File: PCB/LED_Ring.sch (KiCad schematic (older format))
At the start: 60 parts

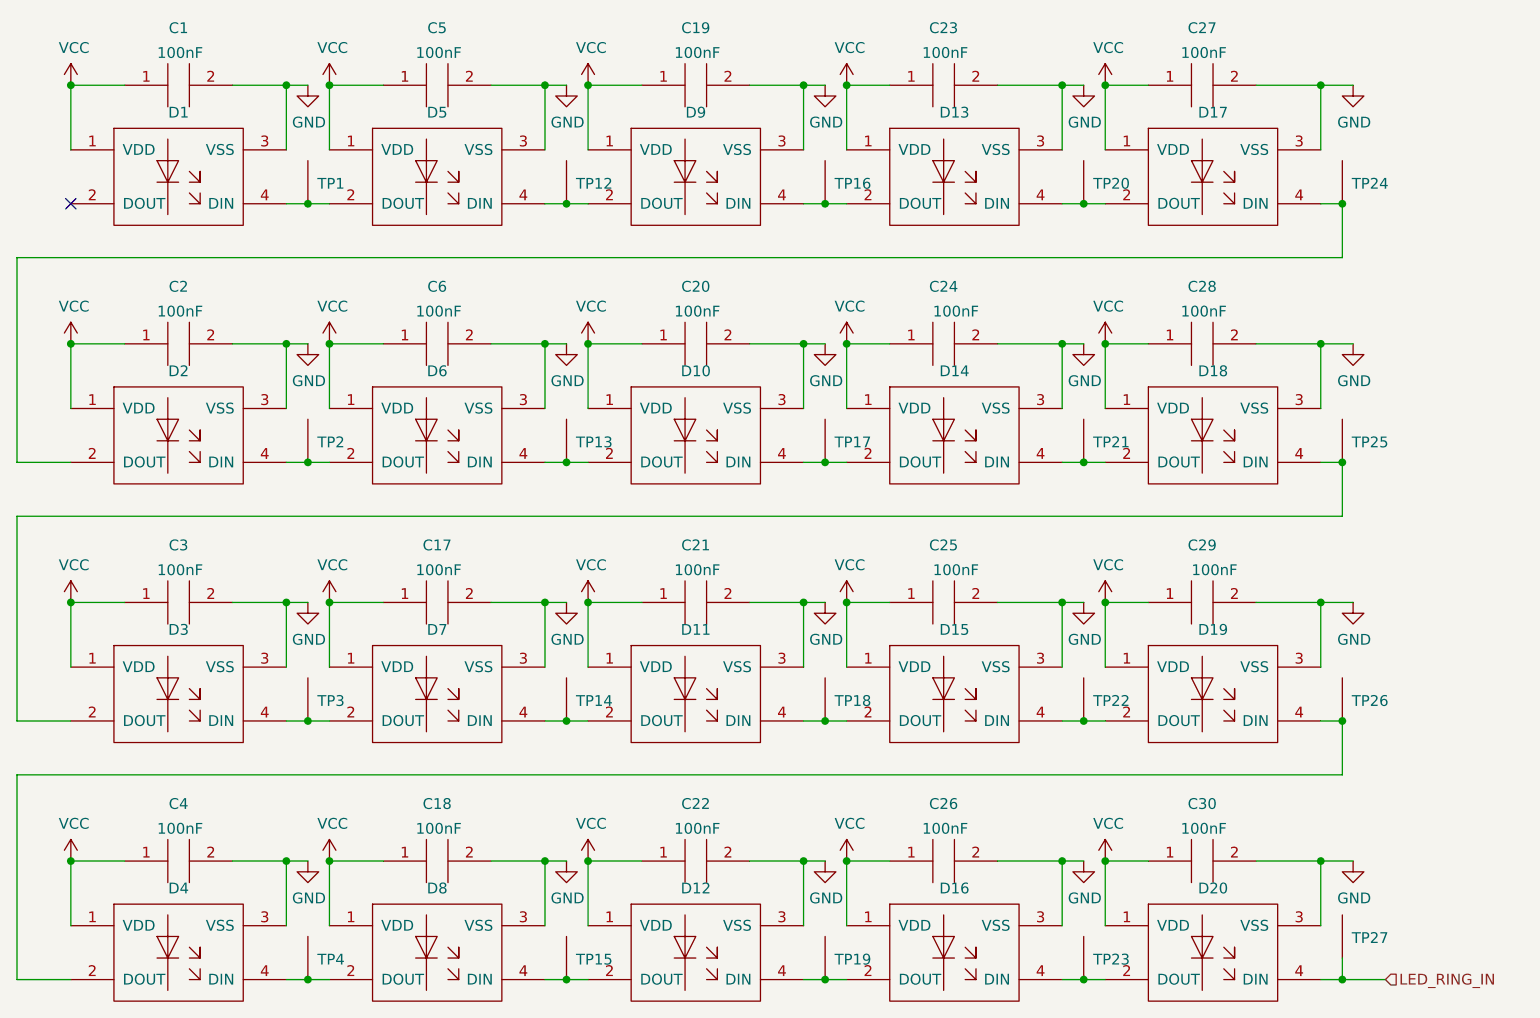
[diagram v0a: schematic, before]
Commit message: Sheet USB
USB Switch und USB Input Stecker hinzugefügt
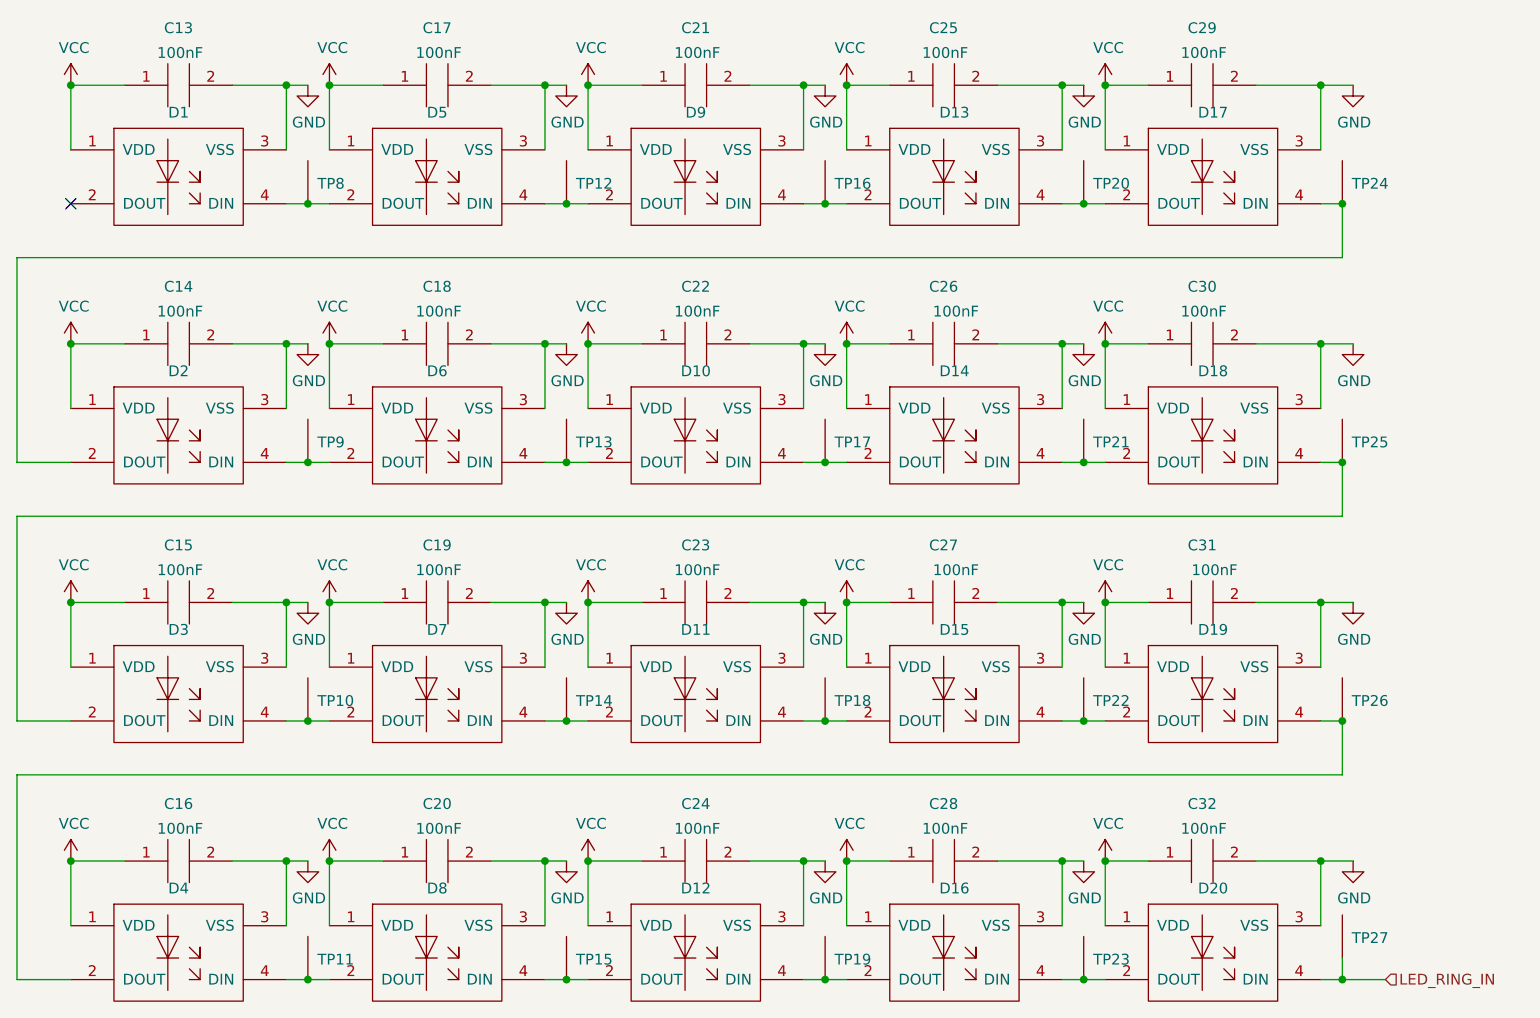
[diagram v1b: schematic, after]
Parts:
- renumbered C1 to C13, C2 to C14, C3 to C15, C4 to C16, C5 to C17, C6 to C18, C17 to C19, C18 to C20, C19 to C21, C20 to C22, C21 to C23, C22 to C24, C23 to C25, C24 to C26, C25 to C27, C26 to C28, C27 to C29, C28 to C30, C29 to C31, C30 to C32, TP3 to TP10, TP4 to TP11, TP1 to TP8, TP2 to TP9
